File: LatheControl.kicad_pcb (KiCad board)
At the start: 2 copper layers, 114.3 x 152.4 mm, 75 parts, among them J1 Conn_01x01, J10 Conn_01x01_Male, J11 Conn_01x01, J12 Conn_01x01, J13 Conn_01x03_Male, J14 Conn_01x02_Male, J15 Conn_01x02_Male, J16 Conn_01x01, J17 Conn_01x01, J18 Conn_01x01_Male, J19 Conn_01x02_Male, J2 Conn_01x01, J20 Conn_01x02_Male, J21 Conn_01x02_Male, J3 Conn_01x01, J4 Conn_01x02_Male, J5 Conn_01x01, J6 Conn_01x01, J7 Conn_01x01_Male, J8 Conn_01x01_Male, J9 Conn_01x01_Male, K1 LY2-0-DC12, K2 LY2-0-DC12, K3 LY2-0-DC12, Q1 Q_NMOS_GSD, Q2 Q_NMOS_GSD, Q3 Q_NMOS_GSD, Q4 Q_NMOS_GSD, Q5 Q_NMOS_GSD, Q6 Q_NMOS_GSD, SW1 SW_Push_SPDT, T1 FS16-150, U1 NCP1117-ADJ_SOT223, U10 74LVC1G08, U2 NCP1117-ADJ_SOT223, U3 74LVC1G08, U4 74AHC1G04, U5 74LVC1G08, U6 74AHC1G04, U7 74LVC1G08, U8 74LVC1G08, U9 74LVC1G08

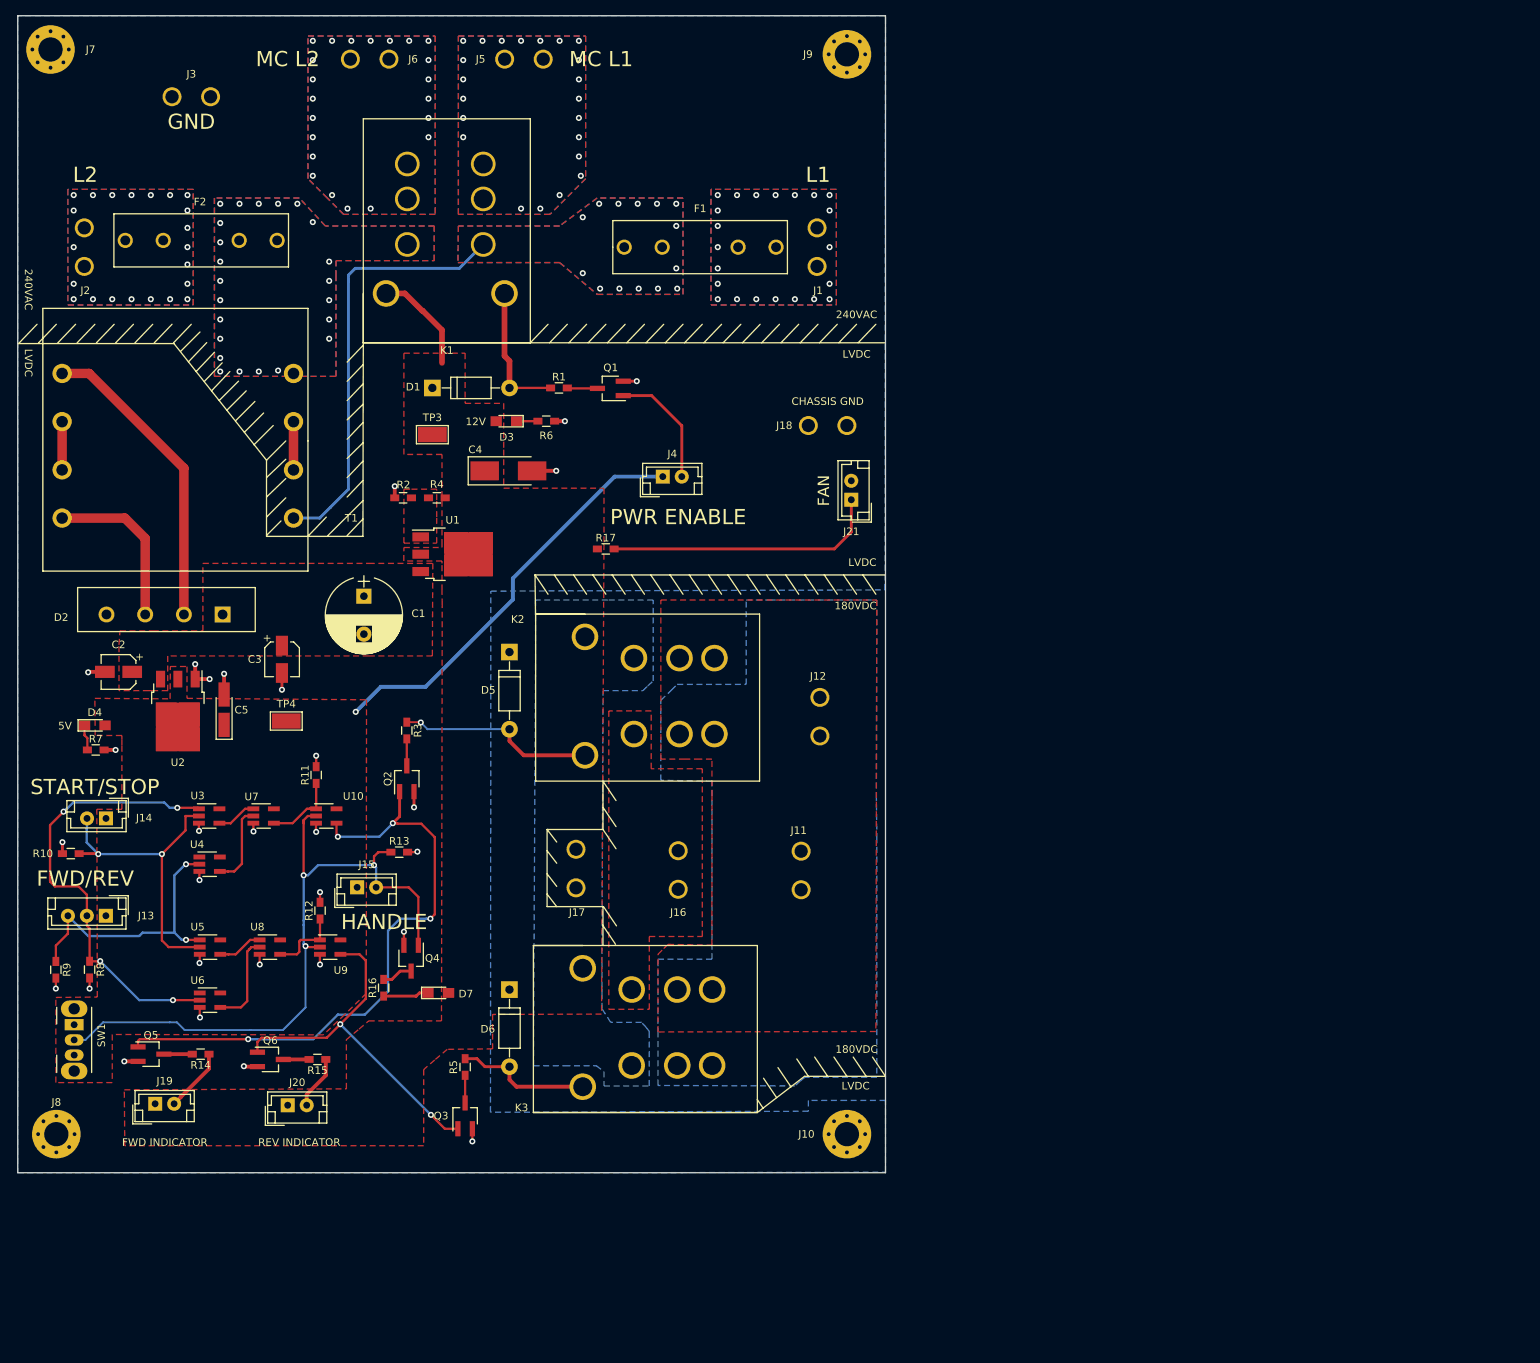
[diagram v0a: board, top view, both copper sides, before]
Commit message: Schematic, board and project files updated with final design notes and board completion. Added part to customFootprints.
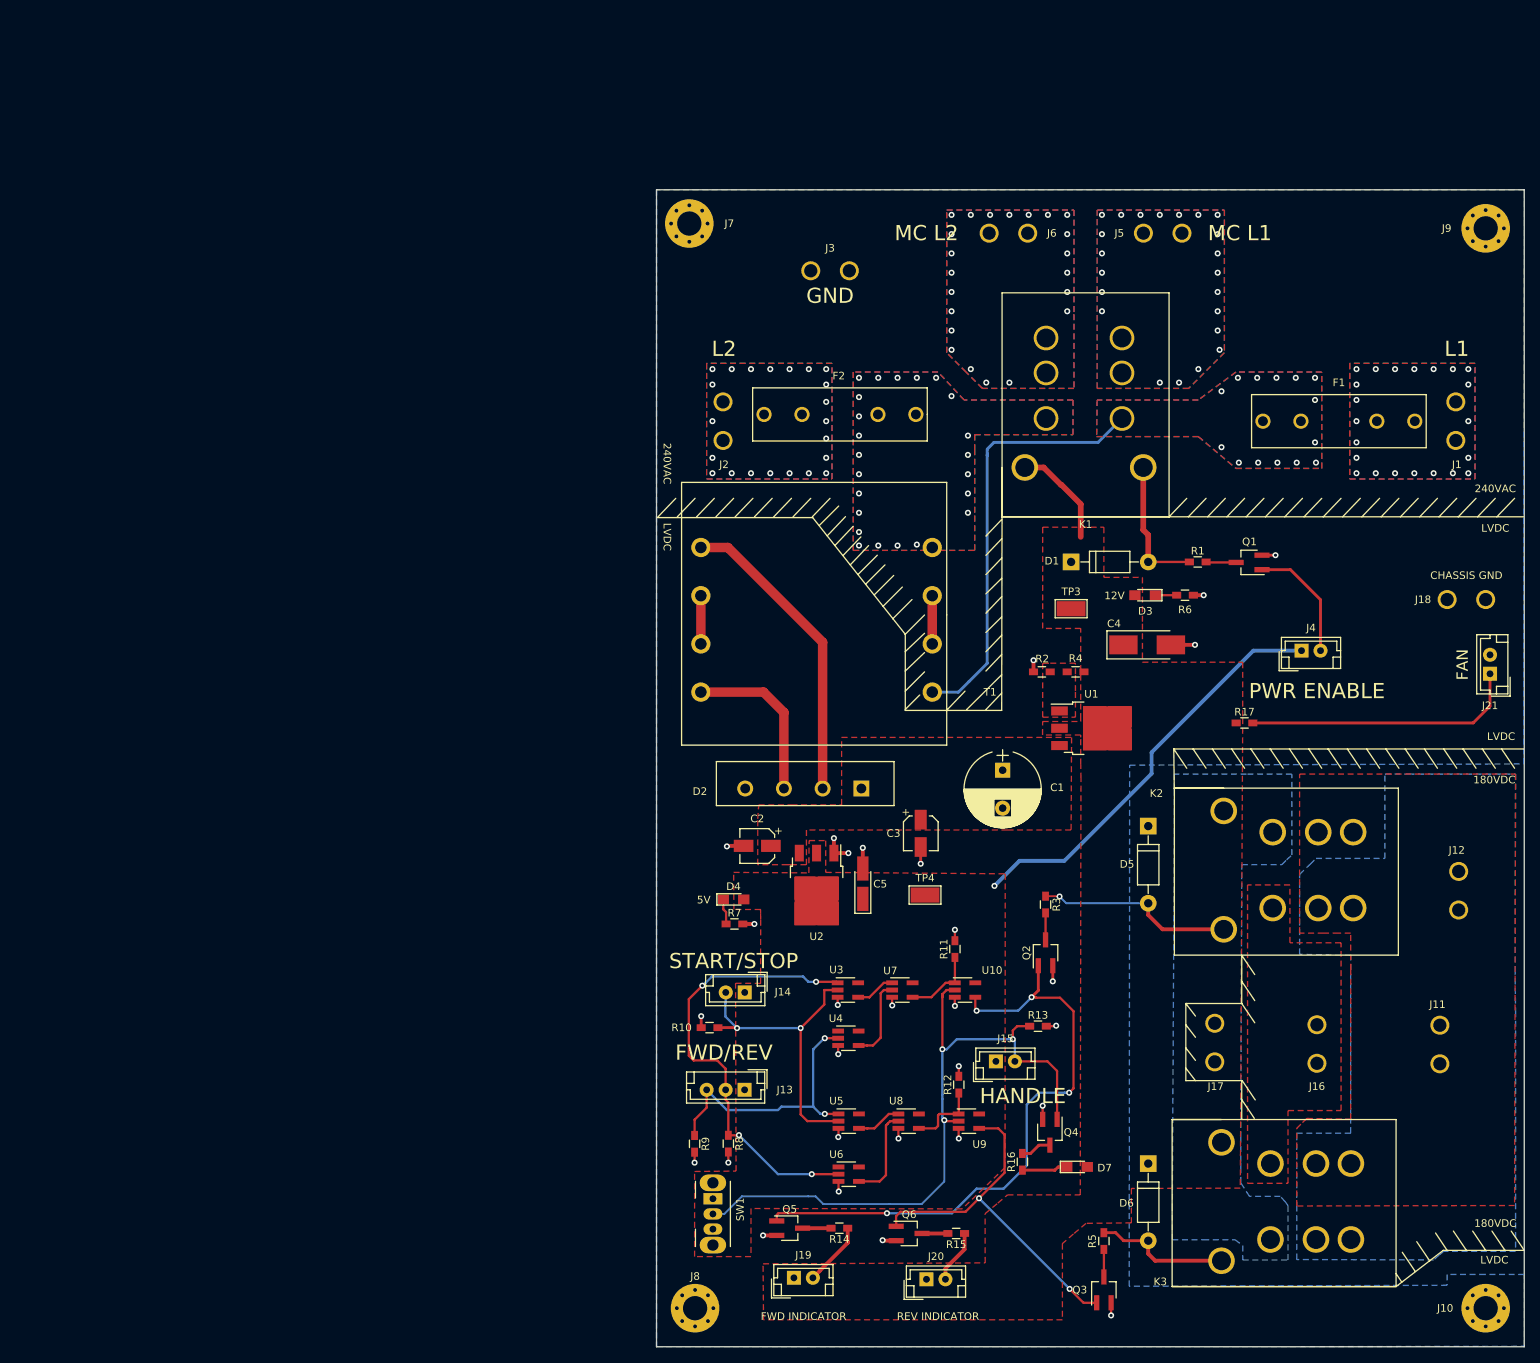
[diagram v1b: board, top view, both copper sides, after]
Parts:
- moved C4 87.2 mm to (225.0, 108.3)
- moved D3 87.2 mm to (224.7, 101.7)
- moved J16 87.2 mm to (247.3, 163.4)
- moved J18 87.2 mm to (264.5, 102.3)
- moved J2 87.2 mm to (169.1, 81.3)
- moved J21 87.2 mm to (270.1, 112.1)
- moved J5 87.2 mm to (229.6, 54.0)
- moved J9 87.2 mm to (269.6, 53.4)
- moved Q3 87.2 mm to (219.3, 193.2)
- moved Q4 87.2 mm to (212.2, 172.5)
- moved R17 87.2 mm to (237.8, 118.6)
- moved R5 87.2 mm to (219.3, 186.8)
- moved R6 87.2 mm to (230.0, 101.7)
- moved R9 87.2 mm to (165.4, 174.0)
- moved C2 87.2 mm to (173.6, 134.7)
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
